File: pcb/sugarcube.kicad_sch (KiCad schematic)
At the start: 0 parts

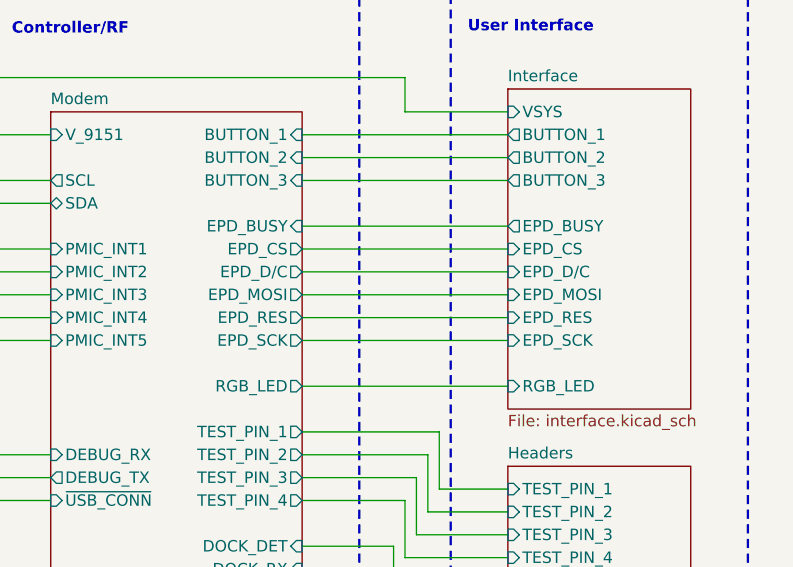
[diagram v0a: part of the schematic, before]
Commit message: Bus for epaper
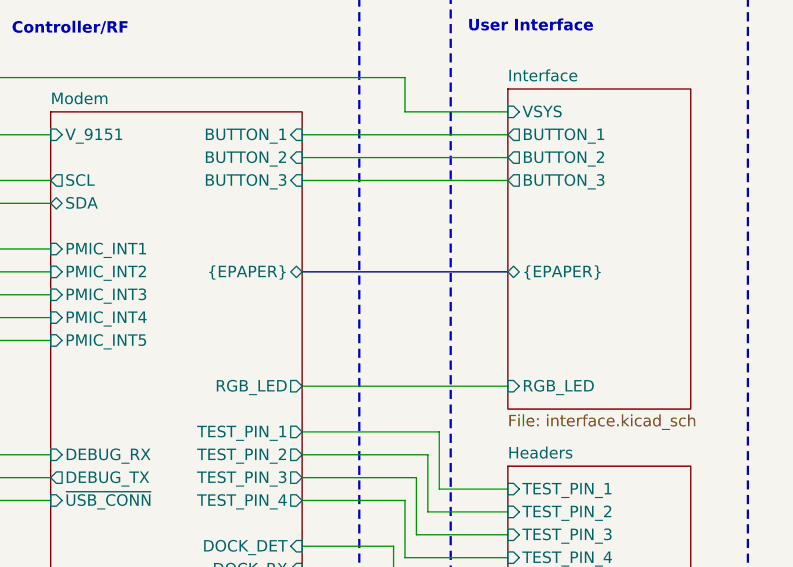
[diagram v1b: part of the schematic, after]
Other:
- sheet Interface ports: added {EPAPER}; removed EPD_BUSY, EPD_CS, EPD_D/C, EPD_MOSI, EPD_RES, EPD_SCK
- sheet Modem ports: added {EPAPER}; removed EPD_BUSY, EPD_CS, EPD_D/C, EPD_MOSI, EPD_RES, EPD_SCK
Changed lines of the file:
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@@
-	(wire
-		(pts
-			(xy 182.88 90.17) (xy 205.74 90.17)
-		)
-		(stroke
-			(width 0)
-			(type default)
-		)
-	)
 	(wire
 		(pts
@@
 	(wire
 		(pts
-			(xy 182.88 85.09) (xy 205.74 85.09)
-		)
-		(stroke
-			(width 0)
-			(type default)
-		)
-	)
-	(wire
-		(pts
 			(xy 196.85 107.95) (xy 196.85 114.3)
 		)
@@
 		)
 	)
-	(wire
+	(bus
 		(pts
 			(xy 182.88 87.63) (xy 205.74 87.63)
@@
 	(wire
 		(pts
-			(xy 182.88 82.55) (xy 205.74 82.55)
-		)
-		(stroke
-			(width 0)
-			(type default)
-		)
-	)
-	(wire
-		(pts
 			(xy 132.08 95.25) (xy 154.94 95.25)
 		)
@@
 	(wire
 		(pts
-			(xy 182.88 95.25) (xy 205.74 95.25)
-		)
-		(stroke
-			(width 0)
-			(type default)
-		)
-	)
-	(wire
-		(pts
 			(xy 132.08 72.39) (xy 143.51 72.39)
 		)
@@
 		(pts
 			(xy 194.31 119.38) (xy 194.31 113.03)
-		)
-		(stroke
-			(width 0)
-			(type default)
-		)
-	)
-	(wire
-		(pts
-			(xy 182.88 92.71) (xy 205.74 92.71)
 		)
 		(stroke
@@
 			)
 		)
-		(pin "EPD_BUSY" input
-			(at 182.88 82.55 0)
-			(effects
-				(font
-					(size 1.27 1.27)
-				)
-				(justify right)
-			)
-		)
-		(pin "EPD_CS" output
-			(at 182.88 85.09 0)
-			(effects
-				(font
-					(size 1.27 1.27)
-				)
-				(justify right)
-			)
-		)
-		(pin "EPD_D{slash}C" output
-			(at 182.88 87.63 0)
-			(effects
-				(font
-					(size 1.27 1.27)
-				)
-				(justify right)
-			)
-		)
-		(pin "EPD_MOSI" output
-			(at 182.88 90.17 0)
-			(effects
-				(font
-					(size 1.27 1.27)
-				)
-				(justify right)
-			)
-		)
-		(pin "EPD_RES" output
-			(at 182.88 92.71 0)
-			(effects
-				(font
-					(size 1.27 1.27)
-				)
-				(justify right)
-			)
-		)
-		(pin "EPD_SCK" output
-			(at 182.88 95.25 0)
-			(effects
-				(font
-					(size 1.27 1.27)
-				)
-				(justify right)
-			)
-		)
 		(pin "PMIC_INT1" input
 			(at 154.94 85.09 180)
@@
 				)
 				(justify left)
+			)
+		)
+		(pin "{EPAPER}" bidirectional
+			(at 182.88 87.63 0)
+			(effects
+				(font
+					(size 1.27 1.27)
+				)
+				(justify right)
 			)
 		)
@@
 			)
 		)
-		(pin "EPD_BUSY" output
-			(at 205.74 82.55 180)
-			(effects
-				(font
-					(size 1.27 1.27)
-				)
-				(justify left)
-			)
-		)
-		(pin "EPD_CS" input
-			(at 205.74 85.09 180)
-			(effects
-				(font
-					(size 1.27 1.27)
-				)
-				(justify left)
-			)
-		)
-		(pin "EPD_D{slash}C" input
-			(at 205.74 87.63 180)
-			(effects
-				(font
-					(size 1.27 1.27)
-				)
-				(justify left)
-			)
-		)
-		(pin "EPD_MOSI" input
-			(at 205.74 90.17 180)
-			(effects
-				(font
-					(size 1.27 1.27)
-				)
-				(justify left)
-			)
-		)
-		(pin "EPD_RES" input
-			(at 205.74 92.71 180)
-			(effects
-				(font
-					(size 1.27 1.27)
-				)
-				(justify left)
-			)
-		)
-		(pin "EPD_SCK" input
-			(at 205.74 95.25 180)
-			(effects
-				(font
-					(size 1.27 1.27)
-				)
-				(justify left)
-			)
-		)
 		(pin "RGB_LED" input
 			(at 205.74 100.33 180)
@@
 			(effects
 				(font
+					(size 1.27 1.27)
+				)
+				(justify left)
+			)
+		)
+		(pin "{EPAPER}" bidirectional
+			(at 205.74 87.63 180)
+			(effects
+				(font
